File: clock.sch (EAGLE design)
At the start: 44 parts, among them J3 POWER_JACKSLT, U2 LM75A_SO8, U3 ESP8266_13

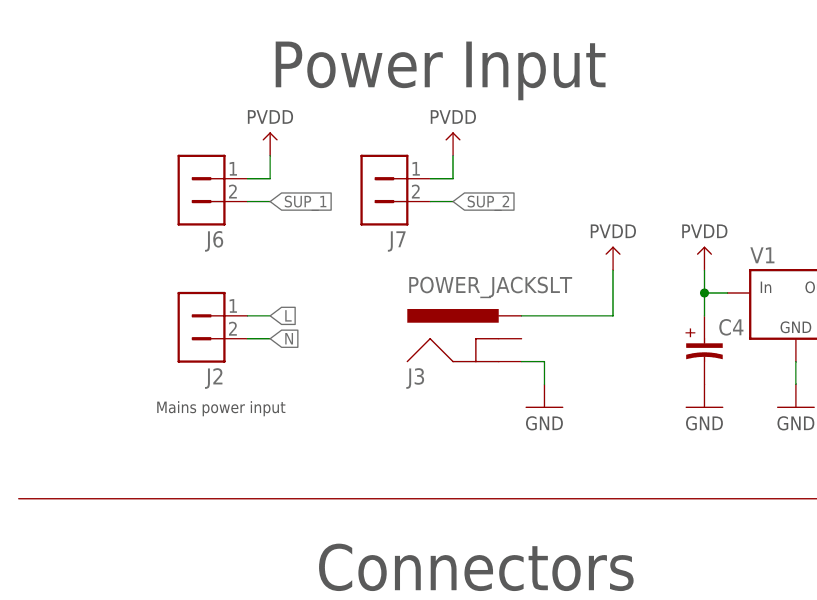
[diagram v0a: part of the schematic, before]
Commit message: Added a power led and some silkscreen to make the footprints for the temperature sensors more obvious
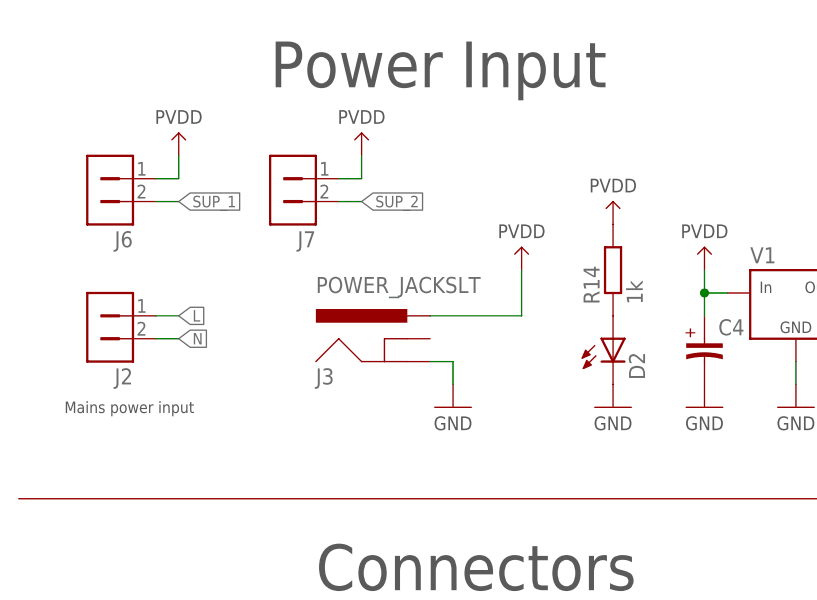
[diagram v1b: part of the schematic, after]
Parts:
- added D2: (no value), Sebastian:LED_0805
- added R14: 1k, Sebastian:R_0603
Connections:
- new net N$4: D2.A, R14.1
- net GND: now also D2.C
- net PVDD: now also R14.2
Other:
- moved on the sheet: J2, J3, J6, J7
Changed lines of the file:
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@@
 <?xml version="1.0" encoding="utf-8"?>
 <!DOCTYPE eagle SYSTEM "eagle.dtd">
-<eagle version="8.0.1">
+<eagle version="8.5.0">
 <drawing>
 <settings>
 <setting alwaysvectorfont="no"/>
+<setting keepoldvectorfont="yes"/>
 <setting verticaltext="up"/>
 </settings>
@@
 <part name="J7" library="Connectors" deviceset="1X2" device=""/>
 <part name="P41" library="aesthetics" deviceset="PVDD" device=""/>
+<part name="D2" library="Sebastian" deviceset="LED" device="_0805"/>
+<part name="R14" library="Sebastian" deviceset="R" device="_0603" value="1k"/>
+<part name="P42" library="aesthetics" deviceset="GND" device=""/>
+<part name="P43" library="aesthetics" deviceset="PVDD" device=""/>
 </parts>
 <sheets>
@@
 powering and controlling a
 Neopixel LED strip.</text>
-<text x="22.86" y="129.54" size="1.27" layer="97" font="vector" align="center-left">Mains power input</text>
+<text x="12.7" y="129.54" size="1.27" layer="97" font="vector" align="center-left">Mains power input</text>
 <text x="134.62" y="162.56" size="1.27" layer="97" font="vector" align="center-left">Optional switch</text>
 </plain>
@@
 <instance part="R5" gate="G$1" x="165.1" y="147.32" rot="R90"/>
 <instance part="R6" gate="G$1" x="182.88" y="147.32" rot="R90"/>
-<instance part="J2" gate="G$1" x="27.94" y="139.7" rot="MR0"/>
+<instance part="J2" gate="G$1" x="17.78" y="139.7" rot="MR0"/>
 <instance part="U3" gate="G$1" x="152.4" y="81.28"/>
 <instance part="JP1" gate="G$1" x="208.28" y="137.16"/>
@@
 <instance part="P13" gate="G$1" x="104.14" y="144.78"/>
 <instance part="P9" gate="G$1" x="83.82" y="144.78"/>
-<instance part="J3" gate="G$1" x="60.96" y="132.08"/>
-<instance part="P6" gate="G$1" x="66.04" y="129.54"/>
-<instance part="P7" gate="G$1" x="73.66" y="144.78"/>
+<instance part="J3" gate="G$1" x="50.8" y="132.08"/>
+<instance part="P6" gate="G$1" x="55.88" y="129.54"/>
+<instance part="P7" gate="G$1" x="63.5" y="144.78"/>
 <instance part="U2" gate="G$1" x="127" y="25.4"/>
 <instance part="J4" gate="G$1" x="86.36" y="76.2"/>
@@
 <instance part="P38" gate="G$1" x="157.48" y="144.78"/>
 <instance part="P39" gate="G$1" x="127" y="144.78"/>
-<instance part="J6" gate="G$1" x="27.94" y="154.94" rot="MR0"/>
-<instance part="P40" gate="G$1" x="35.56" y="157.48"/>
-<instance part="J7" gate="G$1" x="48.26" y="154.94" rot="MR0"/>
-<instance part="P41" gate="G$1" x="55.88" y="157.48"/>
+<instance part="J6" gate="G$1" x="17.78" y="154.94" rot="MR0"/>
+<instance part="P40" gate="G$1" x="25.4" y="157.48"/>
+<instance part="J7" gate="G$1" x="38.1" y="154.94" rot="MR0"/>
+<instance part="P41" gate="G$1" x="45.72" y="157.48"/>
+<instance part="D2" gate="G$1" x="73.66" y="137.16"/>
+<instance part="R14" gate="G$1" x="73.66" y="144.78" rot="R90"/>
+<instance part="P42" gate="G$1" x="73.66" y="129.54"/>
+<instance part="P43" gate="G$1" x="73.66" y="149.86"/>
 </instances>
 <busses>
@@
 <segment>
 <pinref part="J3" gate="G$1" pin="GND"/>
-<wire x1="63.5" y1="134.62" x2="66.04" y2="134.62" width="0.1524" layer="91"/>
-<wire x1="66.04" y1="134.62" x2="66.04" y2="132.08" width="0.1524" layer="91"/>
+<wire x1="53.34" y1="134.62" x2="55.88" y2="134.62" width="0.1524" layer="91"/>
+<wire x1="55.88" y1="134.62" x2="55.88" y2="132.08" width="0.1524" layer="91"/>
 <pinref part="P6" gate="G$1" pin="GND"/>
 </segment>
@@
 <pinref part="P39" gate="G$1" pin="GND"/>
 </segment>
+<segment>
+<pinref part="P42" gate="G$1" pin="GND"/>
+<pinref part="D2" gate="G$1" pin="C"/>
+</segment>
 </net>
 <net name="PVDD" class="0">
@@
 <segment>
 <pinref part="J3" gate="G$1" pin="PWR"/>
-<wire x1="63.5" y1="139.7" x2="73.66" y2="139.7" width="0.1524" layer="91"/>
-<wire x1="73.66" y1="139.7" x2="73.66" y2="144.78" width="0.1524" layer="91"/>
+<wire x1="53.34" y1="139.7" x2="63.5" y2="139.7" width="0.1524" layer="91"/>
+<wire x1="63.5" y1="139.7" x2="63.5" y2="144.78" width="0.1524" layer="91"/>
 <pinref part="P7" gate="G$1" pin="PVDD"/>
 </segment>
 <segment>
 <pinref part="J6" gate="G$1" pin="1"/>
-<wire x1="33.02" y1="154.94" x2="35.56" y2="154.94" width="0.1524" layer="91"/>
-<wire x1="35.56" y1="154.94" x2="35.56" y2="157.48" width="0.1524" layer="91"/>
+<wire x1="22.86" y1="154.94" x2="25.4" y2="154.94" width="0.1524" layer="91"/>
+<wire x1="25.4" y1="154.94" x2="25.4" y2="157.48" width="0.1524" layer="91"/>
 <pinref part="P40" gate="G$1" pin="PVDD"/>
 </segment>
 <segment>
 <pinref part="J7" gate="G$1" pin="1"/>
-<wire x1="53.34" y1="154.94" x2="55.88" y2="154.94" width="0.1524" layer="91"/>
-<wire x1="55.88" y1="154.94" x2="55.88" y2="157.48" width="0.1524" layer="91"/>
+<wire x1="43.18" y1="154.94" x2="45.72" y2="154.94" width="0.1524" layer="91"/>
+<wire x1="45.72" y1="154.94" x2="45.72" y2="157.48" width="0.1524" layer="91"/>
 <pinref part="P41" gate="G$1" pin="PVDD"/>
+</segment>
+<segment>
+<pinref part="R14" gate="G$1" pin="2"/>
+<pinref part="P43" gate="G$1" pin="PVDD"/>
 </segment>
 </net>
@@
 <segment>
 <pinref part="J2" gate="G$1" pin="1"/>
-<wire x1="33.02" y1="139.7" x2="35.56" y2="139.7" width="0.1524" layer="91"/>
-<label x="35.56" y="139.7" size="1.27" layer="95" font="vector" xref="yes"/>
+<wire x1="22.86" y1="139.7" x2="25.4" y2="139.7" width="0.1524" layer="91"/>
+<label x="25.4" y="139.7" size="1.27" layer="95" font="vector" xref="yes"/>
 </segment>
 </net>
@@
 <segment>
 <pinref part="J2" gate="G$1" pin="2"/>
-<wire x1="33.02" y1="137.16" x2="35.56" y2="137.16" width="0.1524" layer="91"/>
-<label x="35.56" y="137.16" size="1.27" layer="95" font="vector" xref="yes"/>
+<wire x1="22.86" y1="137.16" x2="25.4" y2="137.16" width="0.1524" layer="91"/>
+<label x="25.4" y="137.16" size="1.27" layer="95" font="vector" xref="yes"/>
 </segment>
 </net>
@@
 <segment>
 <pinref part="J6" gate="G$1" pin="2"/>
-<wire x1="33.02" y1="152.4" x2="35.56" y2="152.4" width="0.1524" layer="91"/>
-<label x="35.56" y="152.4" size="1.27" layer="95" font="vector" xref="yes"/>
+<wire x1="22.86" y1="152.4" x2="25.4" y2="152.4" width="0.1524" layer="91"/>
+<label x="25.4" y="152.4" size="1.27" layer="95" font="vector" xref="yes"/>
 </segment>
 </net>
@@
 <segment>
 <pinref part="J7" gate="G$1" pin="2"/>
-<wire x1="53.34" y1="152.4" x2="55.88" y2="152.4" width="0.1524" layer="91"/>
-<label x="55.88" y="152.4" size="1.27" layer="95" font="vector" xref="yes"/>
-</segment>
-</net>
+<wire x1="43.18" y1="152.4" x2="45.72" y2="152.4" width="0.1524" layer="91"/>
+<label x="45.72" y="152.4" size="1.27" layer="95" font="vector" xref="yes"/>
+</segment>
+</net>
+<net name="N$4" class="0">
+<segment>
+<pinref part="D2" gate="G$1" pin="A"/>
+<pinref part="R14" gate="G$1" pin="1"/>
+</segment>
+</net>

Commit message: Added a status LED to IO0
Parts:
- added D3: (no value), Sebastian:LED_0805
- added R15: 1k, Sebastian:R_0603
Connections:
- new net N$5: D3.A, R15.1
- net IO0: now also D3.C
- net PVDD: now also R15.2
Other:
- note added: "Decoupling"
- note added: "Power LED"
- note added: "Status LED"
- moved on the sheet: C10, C7, R10, R11, R12, R13, R8, R9, SWT1, SWT2, TP1, U3

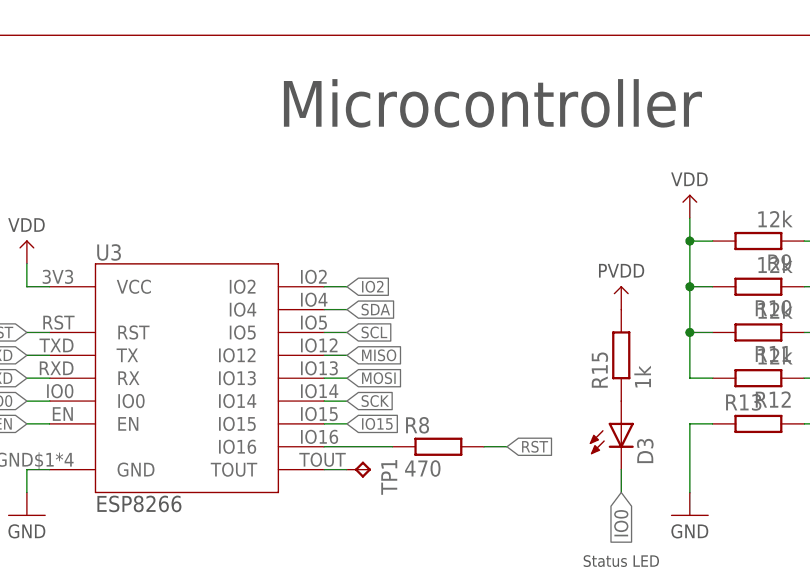
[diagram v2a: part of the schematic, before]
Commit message: Added testpoints to IO2 and IO3
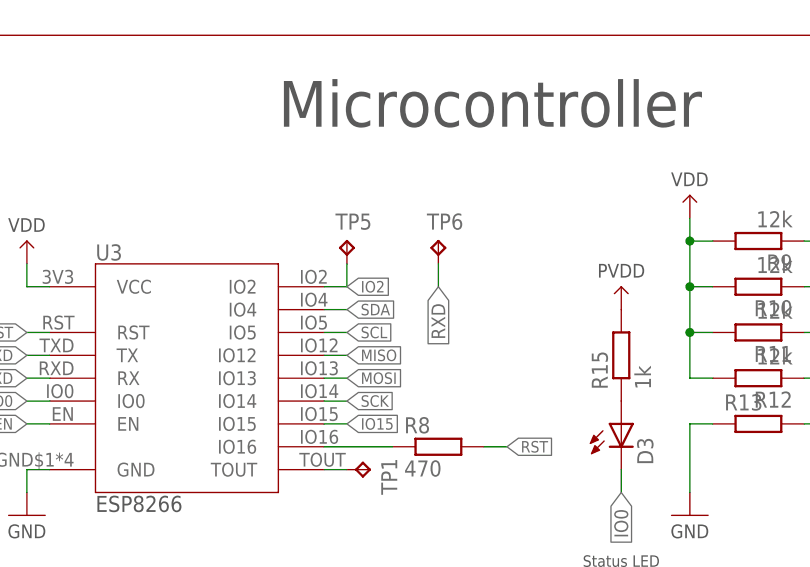
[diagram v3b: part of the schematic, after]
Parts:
- added TP5, TP6: TPTP15R, testpad:TPTP15R
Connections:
- net IO2: now also TP5.TP
- net RXD: now also TP6.TP
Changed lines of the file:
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@@
 <part name="R15" library="Sebastian" deviceset="R" device="_0603" value="1k"/>
 <part name="P44" library="aesthetics" deviceset="PVDD" device=""/>
+<part name="TP5" library="testpad" deviceset="TP" device="TP15R" value="TPTP15R"/>
+<part name="TP6" library="testpad" deviceset="TP" device="TP15R" value="TPTP15R"/>
 </parts>
 <sheets>
@@
 <instance part="R15" gate="G$1" x="198.12" y="83.82" rot="R90"/>
 <instance part="P44" gate="G$1" x="198.12" y="88.9"/>
+<instance part="TP5" gate="G$1" x="167.64" y="96.52"/>
+<instance part="TP6" gate="G$1" x="177.8" y="96.52"/>
 </instances>
 <busses>
@@
 <wire x1="165.1" y1="91.44" x2="167.64" y2="91.44" width="0.1524" layer="91"/>
 <label x="167.64" y="91.44" size="1.27" layer="95" font="vector" xref="yes"/>
+<pinref part="TP5" gate="G$1" pin="TP"/>
+<wire x1="167.64" y1="93.98" x2="167.64" y2="91.44" width="0.1524" layer="91"/>
 </segment>
 <segment>
@@
 <label x="127" y="157.48" size="1.27" layer="95" font="vector" rot="R180" xref="yes"/>
 </segment>
-</net>
+<segment>
+<pinref part="TP6" gate="G$1" pin="TP"/>
+<wire x1="177.8" y1="93.98" x2="177.8" y2="91.44" width="0.1524" layer="91"/>
+<label x="177.8" y="91.44" size="1.524" layer="95" font="vector" rot="R270" xref="yes"/>
+</segment>
+</net>

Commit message: Worked on the silk
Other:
- note added: "Jumpers to disconnect supplies from the input"
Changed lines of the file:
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@@
 <text x="215.9" y="124.46" size="1.27" layer="97" font="vector" align="center-left">Decoupling</text>
 <text x="198.12" y="60.96" size="1.27" layer="97" font="vector" align="center">Status LED</text>
+<text x="12.7" y="121.92" size="1.27" layer="97" font="vector" align="center-left">Jumpers to disconnect supplies from the input</text>
 </plain>
 <instances>

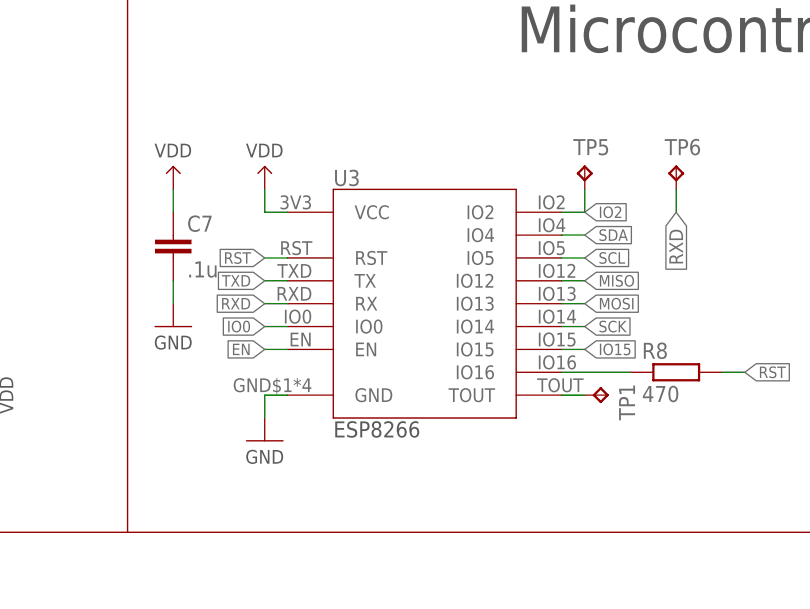
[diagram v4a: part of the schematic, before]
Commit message: Switched to the new footprint for the ESP8266
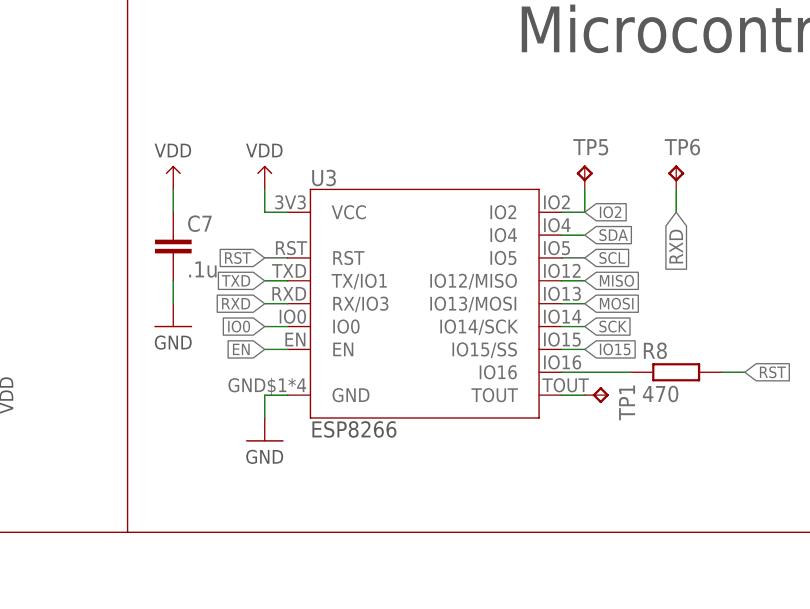
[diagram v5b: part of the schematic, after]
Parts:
- U3: device Sebastian:ESP8266_13 -> Modules:ESP8266_13
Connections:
- net IO15: now also U3.IO15/SS; no longer U3.IO15
- net MISO: now also U3.IO12/MISO; no longer U3.IO12
- net MOSI: now also U3.IO13/MOSI; no longer U3.IO13
- net RXD: now also U3.RX/IO3; no longer U3.RX
- net SCK: now also U3.IO14/SCK; no longer U3.IO14
- net TXD: now also U3.TX/IO1; no longer U3.TX
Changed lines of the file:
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@@
 <layers>
 <layer number="1" name="Top" color="4" fill="1" visible="no" active="no"/>
+<layer number="2" name="Route2" color="1" fill="3" visible="no" active="no"/>
+<layer number="3" name="Route3" color="4" fill="3" visible="no" active="no"/>
+<layer number="4" name="Route4" color="1" fill="4" visible="no" active="no"/>
+<layer number="5" name="Route5" color="4" fill="4" visible="no" active="no"/>
+<layer number="6" name="Route6" color="1" fill="8" visible="no" active="no"/>
+<layer number="7" name="Route7" color="4" fill="8" visible="no" active="no"/>
+<layer number="8" name="Route8" color="1" fill="2" visible="no" active="no"/>
+<layer number="9" name="Route9" color="4" fill="2" visible="no" active="no"/>
+<layer number="10" name="Route10" color="1" fill="7" visible="no" active="no"/>
+<layer number="11" name="Route11" color="4" fill="7" visible="no" active="no"/>
+<layer number="12" name="Route12" color="1" fill="5" visible="no" active="no"/>
+<layer number="13" name="Route13" color="4" fill="5" visible="no" active="no"/>
+<layer number="14" name="Route14" color="1" fill="6" visible="no" active="no"/>
+<layer number="15" name="Route15" color="4" fill="6" visible="no" active="no"/>
 <layer number="16" name="Bottom" color="1" fill="1" visible="no" active="no"/>
 <layer number="17" name="Pads" color="2" fill="1" visible="no" active="no"/>
@@
 <part name="R6" library="Sebastian" deviceset="R" device="_0603" value="10k"/>
 <part name="J2" library="Sebastian" deviceset="1X2" device="_IEC_C8_RIGHT"/>
-<part name="U3" library="Sebastian" deviceset="ESP8266" device="_13"/>
+<part name="U3" library="Modules" deviceset="ESP8266" device="_13"/>
 <part name="JP1" library="Sebastian" deviceset="1X3" device="_MOLEX_53254"/>
 <part name="J5" library="Sebastian" deviceset="1X2" device="_MOLEX_53254"/>
@@
 <part name="P15" library="aesthetics" deviceset="VDD" device=""/>
 <part name="P16" library="aesthetics" deviceset="GND" device=""/>
-<part name="FRAME1" library="frames" deviceset="A4L-LOC" device=""/>
+<part name="FRAME1" library="Frames" deviceset="A4L-LOC" device=""/>
 <part name="U1" library="Sebastian" deviceset="BME280" device=""/>
 <part name="GND2" library="SparkFun-Aesthetics" deviceset="GND" device=""/>
@@
 <part name="C3" library="Sebastian" deviceset="C" device="_0603" value=".1u"/>
 <part name="GND1" library="SparkFun-Aesthetics" deviceset="GND" device=""/>
-<part name="TP1" library="testpad" deviceset="TP" device="TP15R" value="TPTP15R"/>
-<part name="TP2" library="testpad" deviceset="TP" device="TP15R" value="TPTP15R"/>
-<part name="TP3" library="testpad" deviceset="TP" device="TP15R" value="TPTP15R"/>
+<part name="TP1" library="testpad" library_urn="urn:adsk.eagle:library:385" deviceset="TP" device="TP15R" package3d_urn="urn:adsk.eagle:package:27968/1" value="TPTP15R"/>
+<part name="TP2" library="testpad" library_urn="urn:adsk.eagle:library:385" deviceset="TP" device="TP15R" package3d_urn="urn:adsk.eagle:package:27968/1" value="TPTP15R"/>
+<part name="TP3" library="testpad" library_urn="urn:adsk.eagle:library:385" deviceset="TP" device="TP15R" package3d_urn="urn:adsk.eagle:package:27968/1" value="TPTP15R"/>
 <part name="P4" library="aesthetics" deviceset="VDD" device=""/>
 <part name="P5" library="aesthetics" deviceset="VDD" device=""/>
-<part name="TP4" library="testpad" deviceset="TP" device="TP15R" value="TPTP15R"/>
+<part name="TP4" library="testpad" library_urn="urn:adsk.eagle:library:385" deviceset="TP" device="TP15R" package3d_urn="urn:adsk.eagle:package:27968/1" value="TPTP15R"/>
 <part name="U$1" library="Sebastian" deviceset="SWITCH_1P3T" device="_SSSS812201"/>
 <part name="P38" library="aesthetics" deviceset="GND" device=""/>
@@
 <part name="R15" library="Sebastian" deviceset="R" device="_0603" value="1k"/>
 <part name="P44" library="aesthetics" deviceset="PVDD" device=""/>
-<part name="TP5" library="testpad" deviceset="TP" device="TP15R" value="TPTP15R"/>
-<part name="TP6" library="testpad" deviceset="TP" device="TP15R" value="TPTP15R"/>
+<part name="TP5" library="testpad" library_urn="urn:adsk.eagle:library:385" deviceset="TP" device="TP15R" package3d_urn="urn:adsk.eagle:package:27968/1" value="TPTP15R"/>
+<part name="TP6" library="testpad" library_urn="urn:adsk.eagle:library:385" deviceset="TP" device="TP15R" package3d_urn="urn:adsk.eagle:package:27968/1" value="TPTP15R"/>
 </parts>
 <sheets>
@@
 </segment>
 <segment>
-<pinref part="U3" gate="G$1" pin="IO15"/>
+<pinref part="U3" gate="G$1" pin="IO15/SS"/>
 <wire x1="165.1" y1="76.2" x2="167.64" y2="76.2" width="0.1524" layer="91"/>
 <label x="167.64" y="76.2" size="1.27" layer="95" font="vector" xref="yes"/>
@@
 <net name="RXD" class="0">
 <segment>
-<pinref part="U3" gate="G$1" pin="RX"/>
+<pinref part="U3" gate="G$1" pin="RX/IO3"/>
 <wire x1="134.62" y1="81.28" x2="132.08" y2="81.28" width="0.1524" layer="91"/>
 <label x="132.08" y="81.28" size="1.27" layer="95" font="vector" rot="R180" xref="yes"/>
@@
 <net name="TXD" class="0">
 <segment>
-<pinref part="U3" gate="G$1" pin="TX"/>
+<pinref part="U3" gate="G$1" pin="TX/IO1"/>
 <wire x1="134.62" y1="83.82" x2="132.08" y2="83.82" width="0.1524" layer="91"/>
 <label x="132.08" y="83.82" size="1.27" layer="95" font="vector" rot="R180" xref="yes"/>
@@
 <net name="MISO" class="0">
 <segment>
-<pinref part="U3" gate="G$1" pin="IO12"/>
+<pinref part="U3" gate="G$1" pin="IO12/MISO"/>
 <wire x1="165.1" y1="83.82" x2="167.64" y2="83.82" width="0.1524" layer="91"/>
 <label x="167.64" y="83.82" size="1.27" layer="95" font="vector" xref="yes"/>
@@
 <net name="MOSI" class="0">
 <segment>
-<pinref part="U3" gate="G$1" pin="IO13"/>
+<pinref part="U3" gate="G$1" pin="IO13/MOSI"/>
 <wire x1="165.1" y1="81.28" x2="167.64" y2="81.28" width="0.1524" layer="91"/>
 <label x="167.64" y="81.28" size="1.27" layer="95" font="vector" xref="yes"/>
@@
 </segment>
 <segment>
-<pinref part="U3" gate="G$1" pin="IO14"/>
+<pinref part="U3" gate="G$1" pin="IO14/SCK"/>
 <wire x1="165.1" y1="78.74" x2="167.64" y2="78.74" width="0.1524" layer="91"/>
 <label x="167.64" y="78.74" size="1.27" layer="95" font="vector" xref="yes"/>
@@
 which will not be processed correctly with this version.
 </note>
+<note version="8.2" severity="warning">
+Since Version 8.2, EAGLE supports online libraries. The ids
+of those online libraries will not be understood (or retained)
+with this version.
+</note>
+<note version="8.3" severity="warning">
+Since Version 8.3, EAGLE supports URNs for individual library
+assets (packages, symbols, and devices). The URNs of those assets
+will not be understood (or retained) with this version.
+</note>
+<note version="8.3" severity="warning">
+Since Version 8.3, EAGLE supports the association of 3D packages
+with devices in libraries, schematics, and board files. Those 3D
+packages will not be understood (or retained) with this version.
+</note>
 </compatibility>
